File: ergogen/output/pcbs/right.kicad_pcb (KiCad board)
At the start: 2 copper layers, 137 x 110 mm, 79 parts

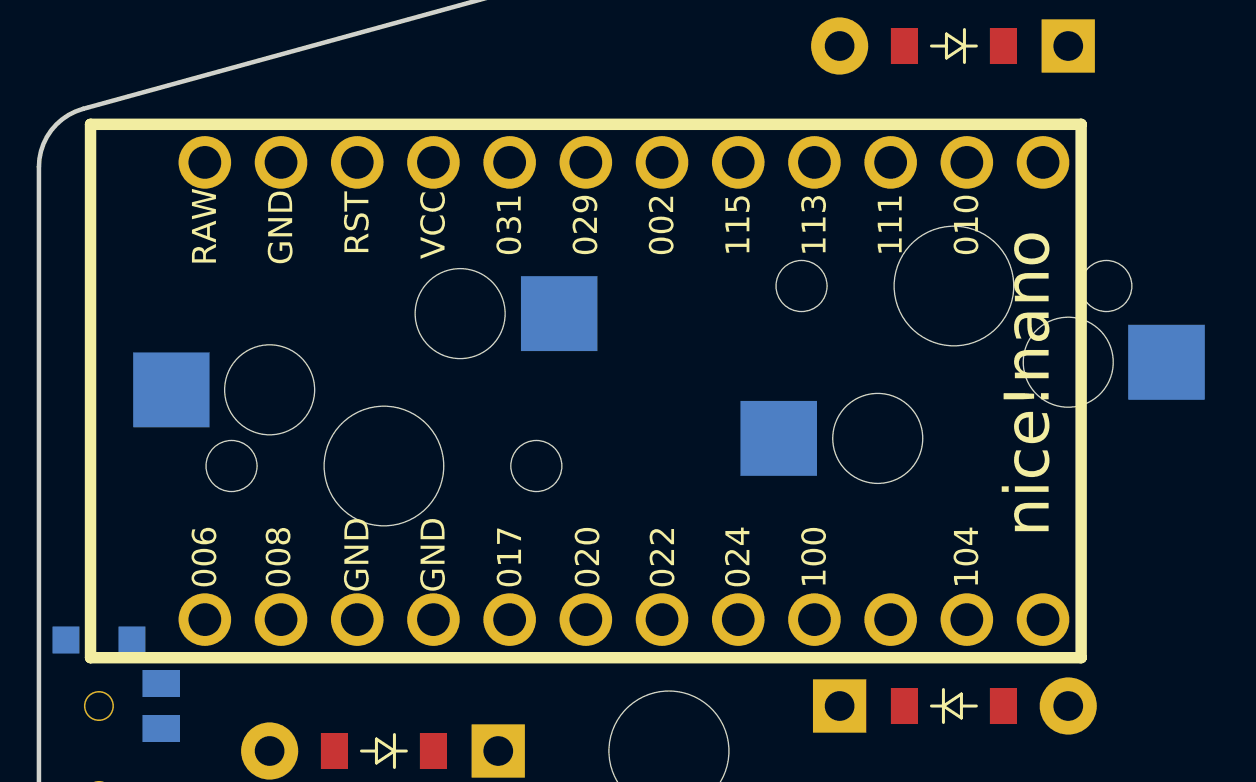
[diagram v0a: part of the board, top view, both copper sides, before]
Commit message: regenned with board flipped correctly; traced pcbs to be redone
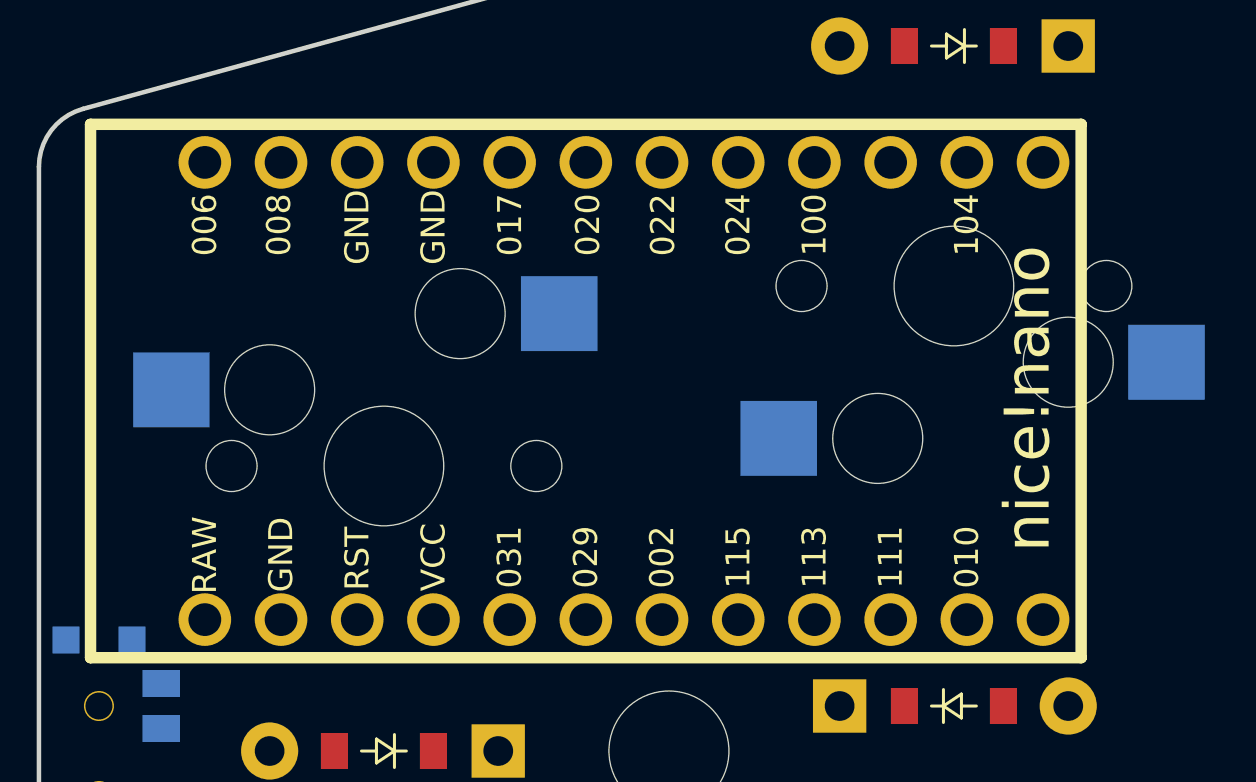
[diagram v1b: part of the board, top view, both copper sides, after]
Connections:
- D1 pad 1: P020 -> P029
- D10 pad 1: P017 -> P031
- D11 pad 1: P020 -> P029
- D12 pad 1: P022 -> P002
- D13 pad 1: P024 -> P115
- D14 pad 1: P100 -> P113
- D15 pad 1: P017 -> P031
- D16 pad 1: P020 -> P029
- D17 pad 1: P022 -> P002
- D18 pad 1: P024 -> P115
- D19 pad 1: P100 -> P113
- D2 pad 1: P022 -> P002
- D20 pad 1: P017 -> P031
- D21 pad 1: P020 -> P029
- D22 pad 1: P022 -> P002
- D23 pad 1: P024 -> P115
- D24 pad 1: P100 -> P113
- D25 pad 1: P017 -> P031
- D26 pad 1: P020 -> P029
- D27 pad 1: P022 -> P002
- D28 pad 1: P024 -> P115
- D29 pad 1: P020 -> P029
- D3 pad 1: P024 -> P115
- D30 pad 1: P022 -> P002
- D31 pad 1: P024 -> P115
- D32 pad 1: P100 -> P113
- D33 pad 1: P017 -> P031
- D34 pad 1: P017 -> P031
- D35 pad 1: P100 -> P113
- D4 pad 1: P100 -> P113
- D5 pad 1: P017 -> P031
- D6 pad 1: P020 -> P029
- D7 pad 1: P022 -> P002
- D8 pad 1: P024 -> P115
- D9 pad 1: P100 -> P113
- S1 pad 1: P002 -> P024
- S10 pad 1: P115 -> P100
- S11 pad 1: P113 -> P011
- S12 pad 1: P113 -> P011
- S13 pad 1: P113 -> P011
- S14 pad 1: P113 -> P011
- S15 pad 1: P113 -> P011
- S16 pad 1: P011 -> P104
- S17 pad 1: P011 -> P104
- S18 pad 1: P011 -> P104
- S19 pad 1: P011 -> P104
- S2 pad 1: P002 -> P024
- S20 pad 1: P011 -> P104
- S21 pad 1: P010 -> P106
- S22 pad 1: P010 -> P106
- S23 pad 1: P010 -> P106
- S24 pad 1: P010 -> P106
- S25 pad 1: P010 -> P106
- S26 pad 1: P009 -> P020
- S27 pad 1: P009 -> P020
- S28 pad 1: P009 -> P020
- S29 pad 1: P031 -> P017
- S3 pad 1: P002 -> P024
- S30 pad 1: P031 -> P017
- S31 pad 1: P031 -> P017
- S32 pad 1: P031 -> P017
- S33 pad 1: P009 -> P020
- S34 pad 1: P009 -> P020
- S35 pad 1: P031 -> P017
- S4 pad 1: P002 -> P024
- S5 pad 1: P002 -> P024
- S6 pad 1: P115 -> P100
- S7 pad 1: P115 -> P100
- S8 pad 1: P115 -> P100
- S9 pad 1: P115 -> P100

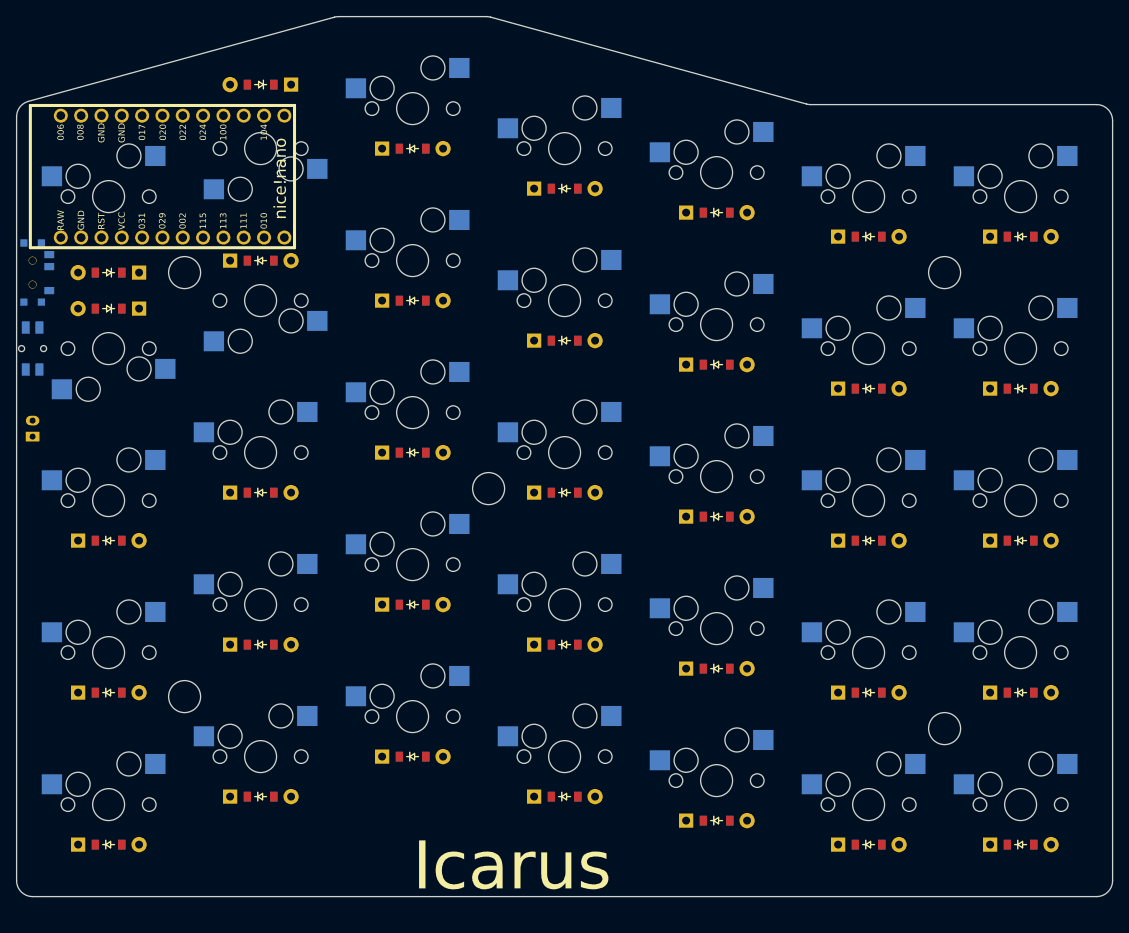
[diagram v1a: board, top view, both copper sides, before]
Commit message: regen board with custom footprints to have 3d models autogenned
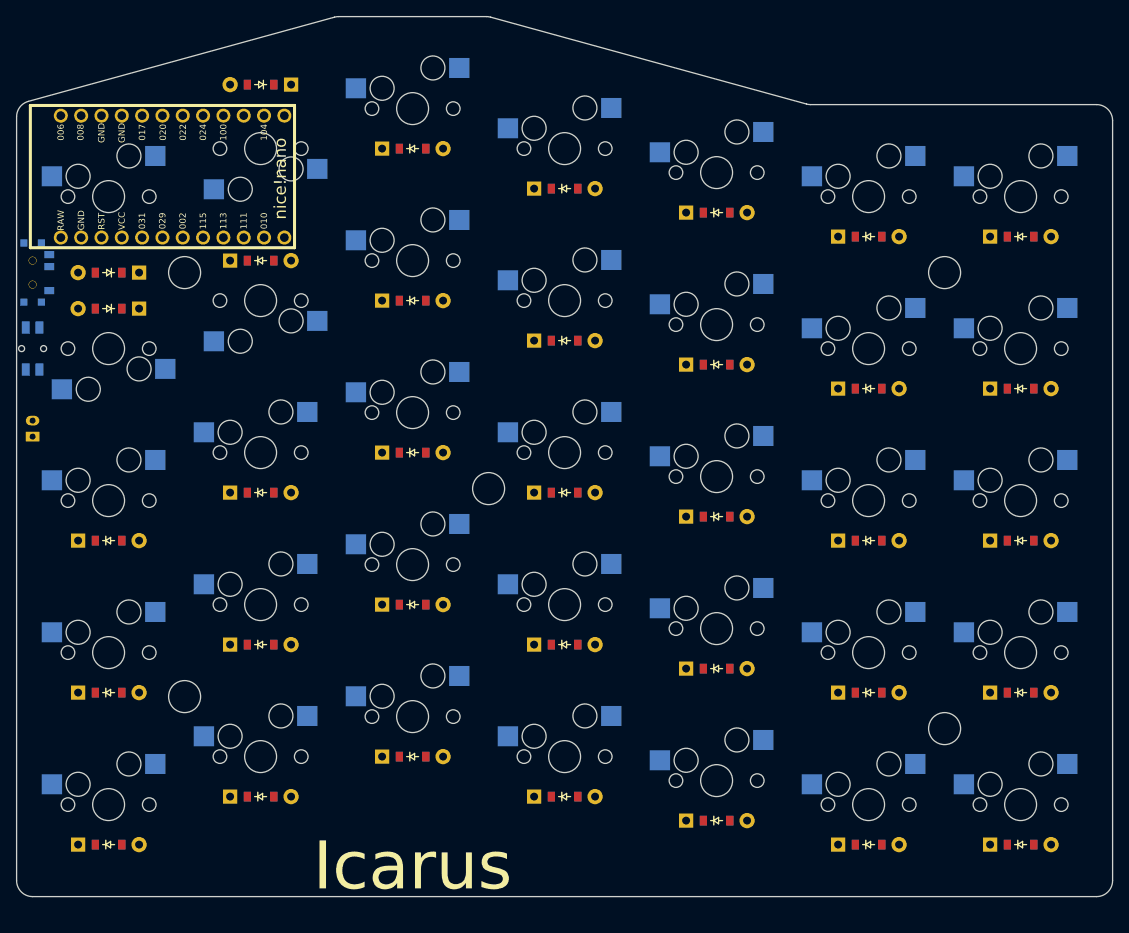
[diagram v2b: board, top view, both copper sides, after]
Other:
- net class Default removed
